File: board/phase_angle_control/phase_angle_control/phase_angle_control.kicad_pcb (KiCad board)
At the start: 4 copper layers, 77.7 x 63.7 mm, 39 parts, among them J1 TB005-762-02BE, J2 TB005-762-02BE, J3 Conn_01x07, J4 Conn_02x04_Odd_Even, J5 Conn_02x04_Odd_Even, J6 Conn_02x04_Odd_Even, J9 Screw_Terminal_01x02, T1 Transformer_1P_1S, U1 STM32G030F6P, U2 PC3H4, U3 MOC3063S-TA1, U4 ACS71240, U7 MAX31855KASA+T

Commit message: Wip3
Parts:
- moved R4 2.66 mm to (114.9, 83.8)
- moved R2 2.48 mm to (118.1, 83.9)
- moved U2 2.33 mm to (116.7, 75.5)
- moved U3 2.22 mm to (124.3, 75.6)
- moved R3 1.95 mm to (125.8, 83.5)
- moved C6 0.60 mm to (132.9, 80.7)
- moved R10 0.41 mm to (135.1, 83.3)
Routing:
- net GND: track 39.1 -> 43.1 mm
- net CURRENT_SENS: track 34.0 -> 30.3 mm
- net zero_crossing: track 49.5 -> 53.1 mm
- net Net-(TRI1-Pad3): track 9.84 -> 12.4 mm
- net AC1: track 26.4 -> 28.3 mm
- net Net-(R3-Pad1): track 3.21 -> 4.81 mm
- net Net-(R1-Pad2): track 3.09 -> 4.37 mm
- net AC2: track 58.9 -> 60.1 mm, vias 26 -> 34
- net Net-(R10-Pad2): track 2.02 -> 2.62 mm
- net AC_LOAD1: vias 16 -> 13
- net AC_LOAD0: vias 14 -> 29
- added copper zone on B.Cu, net +3V3
- added copper zone on F.Cu, net GND

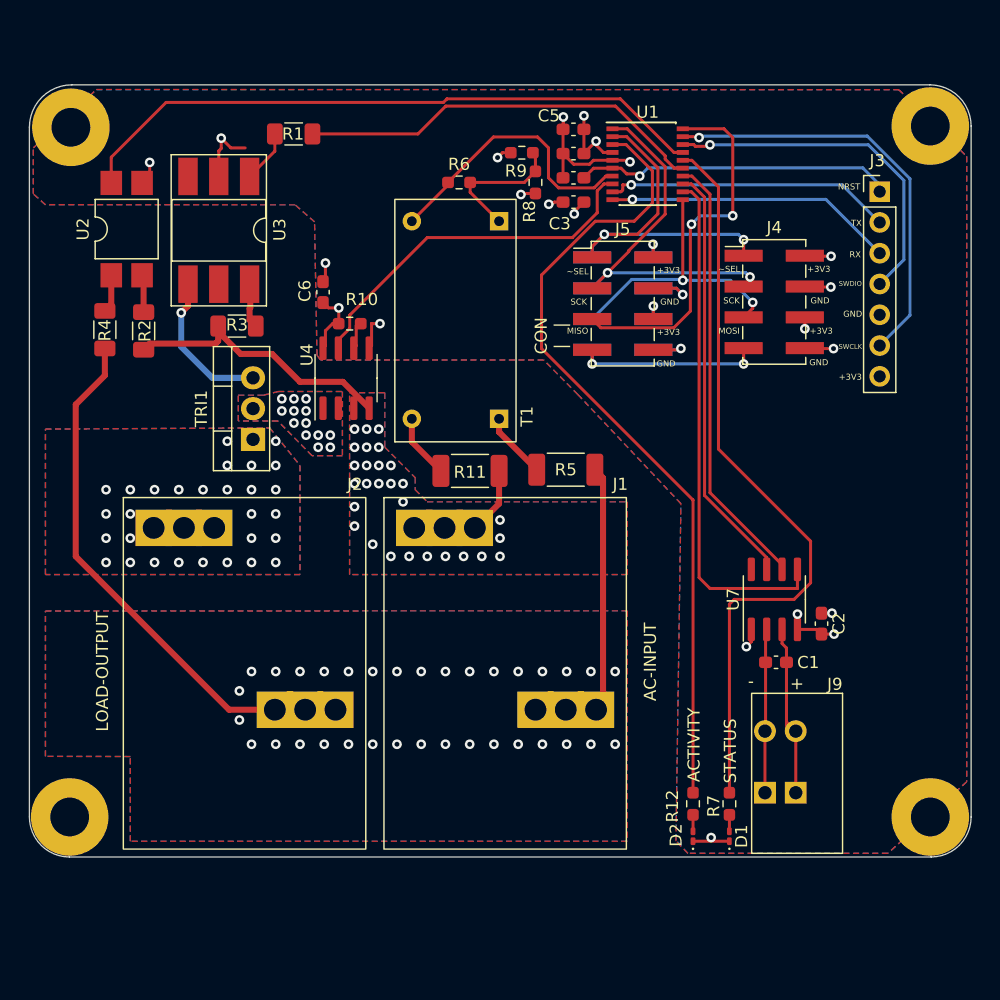
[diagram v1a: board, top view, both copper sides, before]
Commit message: Redesign phase angle contrller board for more current throughput
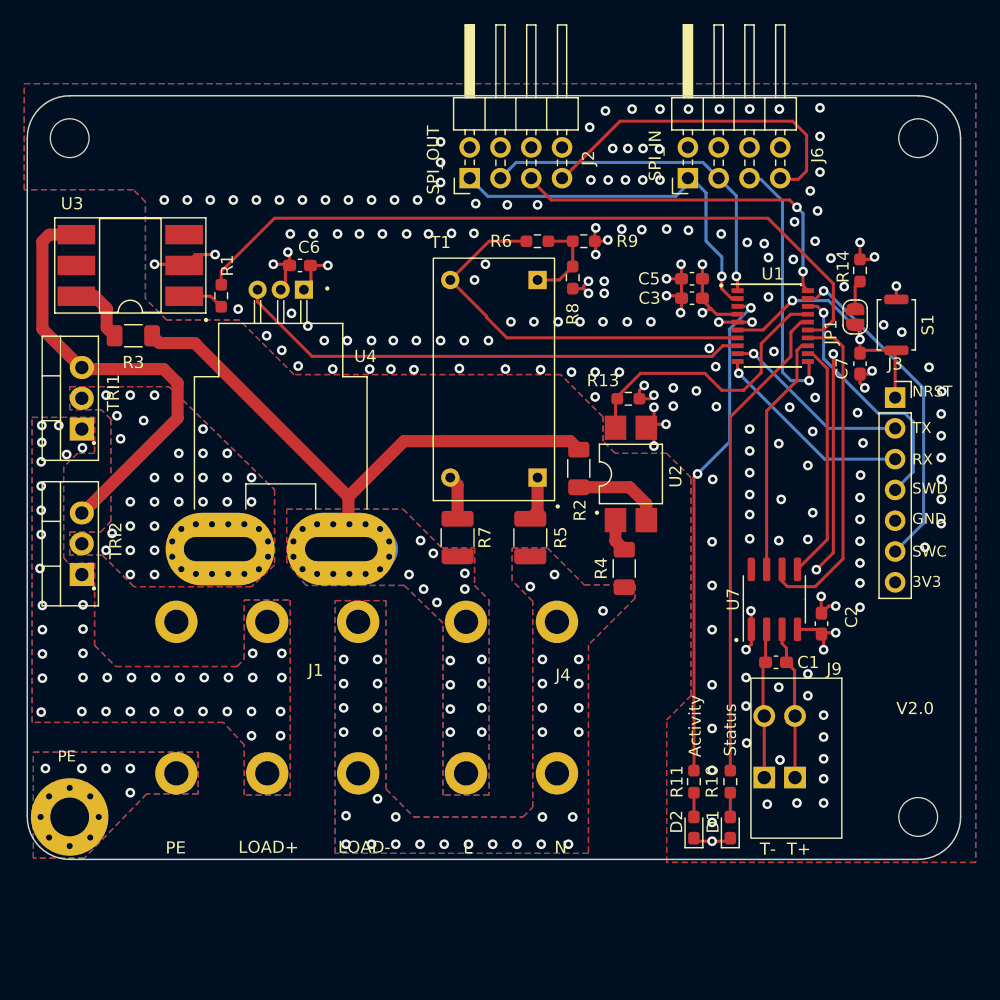
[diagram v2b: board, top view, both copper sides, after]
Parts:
- removed ? (x3): , 
- removed C4: 100nF, Capacitor_SMD:C_0603_1608Metric_Pad1.08x0.95mm_HandSolder
- removed J5: Conn_02x04_Odd_Even, Connector_PinHeader_2.54mm:PinHeader_2x04_P2.54mm_Vertical_SMD
- removed R12: 110, Resistor_SMD:R_0603_1608Metric_Pad0.98x0.95mm_HandSolder
- removed REF**: MountingHole_3.2mm_M3_Pad, MountingHole:MountingHole_3.2mm_M3_Pad
- added JP1: Jumper_2_Open, Jumper:SolderJumper-2_P1.3mm_Open_RoundedPad1.0x1.5mm, F.Cu at (176.8, 82.8)
- added M1: MountingHoles, pac:MountingHolesPE, F.Cu at (112.0, 124.0)
- added R13: 47k, Resistor_SMD:R_0603_1608Metric_Pad0.98x0.95mm_HandSolder, F.Cu at (158.1, 89.5)
- added R14: 330, Resistor_SMD:R_0603_1608Metric_Pad0.98x0.95mm_HandSolder, F.Cu at (177.2, 78.9)
- added S1: B3U-1000P, Button_Switch_SMD:SW_Push_SPST_NO_Alps_SKRK, F.Cu at (180.2, 83.4)
- added TRI2: RS3035H-8A, Package_TO_SOT_THT:TO-220-3_Vertical, F.Cu at (113.0, 104.0)
- D1: value LED_green -> Status; footprint LED_SMD:LED_0201_0603Metric_Pad0.64x0.40mm_HandSolder -> LED_SMD:LED_0603_1608Metric_Pad1.05x0.95mm_HandSolder
- D2: value LED_yellow -> Activity; footprint LED_SMD:LED_0201_0603Metric_Pad0.64x0.40mm_HandSolder -> LED_SMD:LED_0603_1608Metric_Pad1.05x0.95mm_HandSolder
- J1: value TB005-762-02BE -> Screw_Terminal_01x03; footprint pac:con_EB167A-02-H -> pac:KF206B-7.5-3P
- J2: value TB005-762-02BE -> Conn_02x04_Odd_Even; footprint pac:con_EB167A-02-H -> Connector_PinHeader_2.54mm:PinHeader_2x04_P2.54mm_Horizontal
- J3: value Conn_01x07 -> A2541HWV-7P; footprint Connector_PinHeader_2.54mm:PinHeader_1x07_P2.54mm_Vertical -> Connector_PinSocket_2.54mm:PinSocket_1x07_P2.54mm_Vertical
- J4: value Conn_02x04_Odd_Even -> Screw_Terminal_01x02; footprint Connector_PinHeader_2.54mm:PinHeader_2x04_P2.54mm_Vertical_SMD -> pac:KF206B-7.5-2P
- J6: footprint Connector_PinHeader_2.54mm:PinHeader_2x04_P2.54mm_Vertical_SMD -> Connector_PinHeader_2.54mm:PinHeader_2x04_P2.54mm_Horizontal; moved to F.Cu
- J9: value Screw_Terminal_01x02 -> 1-2834016-2
- R1: value 330 -> 110; footprint Resistor_SMD:R_1206_3216Metric_Pad1.30x1.75mm_HandSolder -> Resistor_SMD:R_0603_1608Metric_Pad0.98x0.95mm_HandSolder
- R10: value 10k -> 110
- R11: value 162k -> 110; footprint Resistor_SMD:R_2010_5025Metric_Pad1.40x2.65mm_HandSolder -> Resistor_SMD:R_0603_1608Metric_Pad0.98x0.95mm_HandSolder
- R3: value 330 -> 619
- R5: value 162k -> 280k; footprint Resistor_SMD:R_2010_5025Metric_Pad1.40x2.65mm_HandSolder -> Resistor_SMD:R_1210_3225Metric_Pad1.30x2.65mm_HandSolder
- R6: value 1650 -> 1600
- R7: value 110 -> 280k; footprint Resistor_SMD:R_0603_1608Metric_Pad0.98x0.95mm_HandSolder -> Resistor_SMD:R_1210_3225Metric_Pad1.30x2.65mm_HandSolder
- TRI1: value BTA16-600BWRG -> RS3035H-8A
- U2: value PC3H4 -> EL354N(A)(TA)-VG
- U3: value MOC3063S-TA1 -> MOC3052S-TA1
- U4: value ACS71240 -> ACS758xCB-050B-PFF; footprint Package_SO:SOIC-8_3.9x4.9mm_P1.27mm -> Sensor_Current:Allegro_CB_PFF
- moved R10 49.1 mm to (166.5, 121.1), turned to -90 degrees
- moved R4 47.2 mm to (157.8, 103.5)
- moved U2 46.2 mm to (158.3, 95.7)
- moved J2 44.4 mm to (145.0, 71.3), turned to 90 degrees
- moved J4 39.5 mm to (148.7, 114.7)
- moved R2 37.7 mm to (154.0, 95.2), turned to 90 degrees
- moved R11 31.6 mm to (163.5, 121.1), turned to -90 degrees
- moved R7 31.4 mm to (144.0, 101.0)
- moved C7 28.2 mm to (177.2, 86.6), turned to -90 degrees
- moved J1 19.8 mm to (128.3, 114.3)
- moved J3 17.0 mm to (180.1, 89.4)
- moved U1 16.9 mm to (170.0, 83.5)
- moved C5 15.7 mm to (163.3, 79.6)
- moved R1 14.6 mm to (124.5, 81.0), turned to -90 degrees
- moved TRI1 14.2 mm to (113.0, 92.0)
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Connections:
- J1 pad 1: AC1 -> PE
- J1 pad 2: AC2 -> AC_LOAD0
- J2 pad 1: AC_LOAD0 -> SPI_SEL
- J2 pad 2: AC2 -> +3V3
- J4 pad 1: SPI_SEL -> AC1
- J4 pad 2: +3V3 -> AC2
- J6 pad 1: +3V3 -> SPI_SEL
- J6 pad 2: SPI_SEL -> +3V3
- J6 pad 3: GND -> SPI_SCK
- J6 pad 4: SPI_SCK -> GND
- J6 pad 5: +3V3 -> SPI_MOSI
- J6 pad 6: SPI_MOSI -> +3V3
- J6 pad 7: GND -> RET_MISO
- J6 pad 8: RET_MISO -> GND
- R10 pad 1: +3V3 -> Net-(R10-Pad1)
- R10 pad 2: Net-(R10-Pad2) -> Net-(D1-Pad2)
- R11 pad 1: AC1 -> Net-(R11-Pad1)
- R11 pad 2: Net-(T1-Pad2) -> Net-(D2-Pad2)
- R7 pad 1: Net-(D1-Pad2) -> AC1
- T1 pad 2: Net-(T1-Pad2) -> Net-(R7-Pad2)
- U1 pad 16: Net-(R7-Pad2) -> Net-(R10-Pad1)
- U1 pad 3: Net-(R12-Pad2) -> Net-(R11-Pad1)
- U4 pad 1: AC_LOAD1 -> +3V3
- U4 pad 2: AC_LOAD1 -> GND
- U4 pad 3: AC1 -> CURRENT_SENS
- U4 pad 4: AC1 -> AC_LOAD1
- U4 pad 5: GND -> AC1
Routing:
- net Net-(R12-Pad2): track 66.3 -> 0.00 mm
- net AC2: track 60.1 -> 0.00 mm
- net Net-(R7-Pad2): track 62.6 -> 3.65 mm
- net Net-(R11-Pad1): track 0.00 -> 41.3 mm, vias 0 -> 2
- net Net-(R10-Pad1): track 0.00 -> 40.0 mm
- net zero_crossing: track 53.1 -> 23.4 mm
- net enable_power: track 33.8 -> 61.1 mm
- net Net-(TRI1-Pad3): track 12.4 -> 37.3 mm, vias 1 -> 0
- net AC1: track 28.3 -> 51.8 mm, vias 28 -> 15
- net /Untitled Sheet/CLK: track 42.9 -> 19.3 mm
- net /Untitled Sheet/MISO: track 35.1 -> 20.2 mm
- net CURRENT_SENS: track 30.3 -> 42.8 mm
- net RET_MISO: track 16.1 -> 27.6 mm, vias 2 -> 0
- net VOLTAGE_SENS: track 23.1 -> 33.3 mm
- net GND: track 43.1 -> 52.5 mm, vias 14 -> 189
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- added copper zone on In2.Cu, net +3V3
- added copper zone on B.Cu, net GND
- added copper zone on In1.Cu, net GND
- added copper zone on B.Cu, net PE
- added copper zone on F.Cu, net PE
- added copper zone on In1.Cu, net PE
- added copper zone on In2.Cu, net PE
- removed copper zone on B.Cu, net +3V3
- removed copper zone on In1.Cu, net +3V3
- removed copper zone on In2.Cu, net GND
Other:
- board size 77.7 x 63.7 mm -> 77 x 63 mm
- board text added: "3V3"
- board text added: "CLK"
- board text added: "L"
- board text added: "LOAD+"
- board text added: "LOAD-"
- board text added: "MISO_RET"
- board text added: "N"
- board text added: "PE"
- board text added: "SWC"
- board text added: "SWD"
- board text added: "T+"
- board text added: "T-"
- board text added: "V2.0"
- board text removed: "+"
- board text removed: "+3V3"
- board text removed: "-"
- board text removed: "CON | |"
- board text removed: "SCK"
- board text removed: "SWCLK"
- board text removed: "SWDIO"

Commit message: Update phase-angle-control-board to handle more current
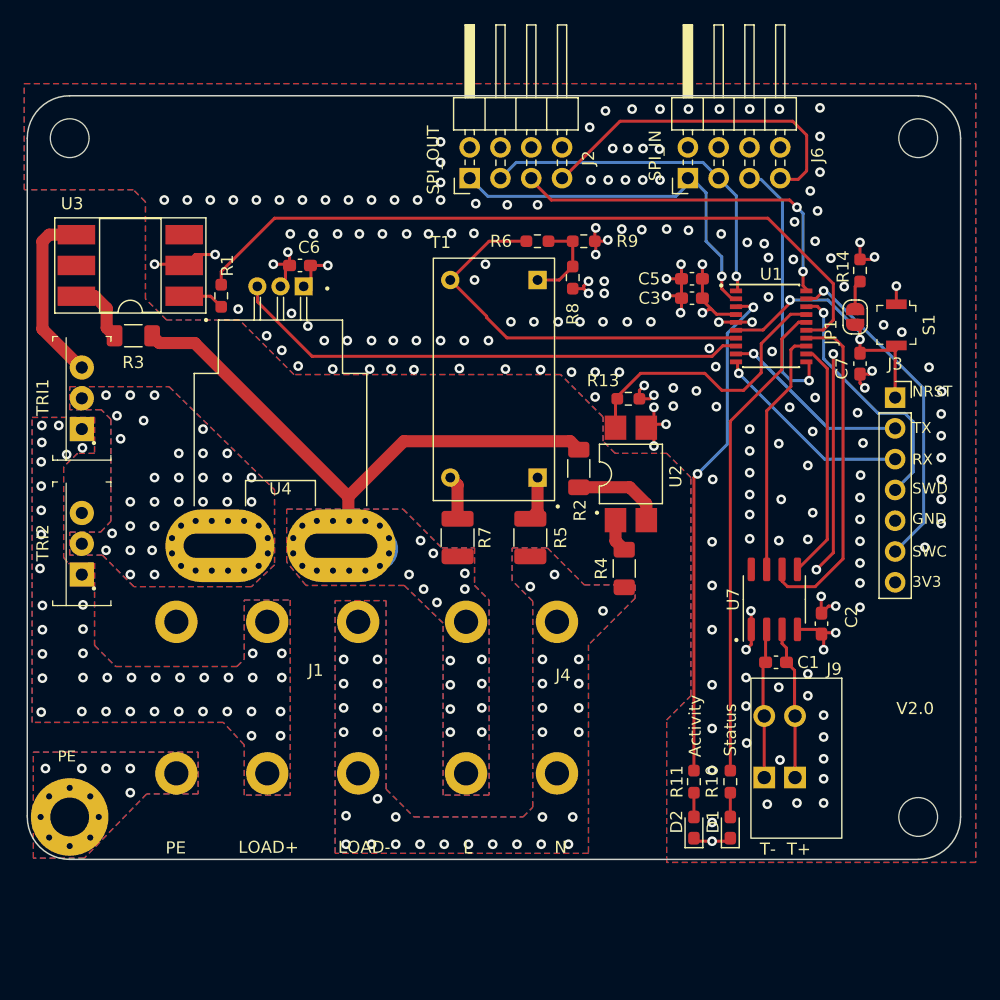
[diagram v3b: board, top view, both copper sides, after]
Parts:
- S1: footprint Button_Switch_SMD:SW_Push_SPST_NO_Alps_SKRK -> digikey-footprints:Switch_Tactile_SMD_B3U-1000P
- TRI1, TRI2: footprint Package_TO_SOT_THT:TO-220-3_Vertical -> digikey-footprints:TO-220-3
- moved U4 0.28 mm to (131.3, 80.2)
- moved U1 0.13 mm to (169.9, 83.5)
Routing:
- net Net-(C1-Pad2): track 13.6 -> 12.7 mm
- net /Untitled Sheet/MISO: track 20.2 -> 20.9 mm

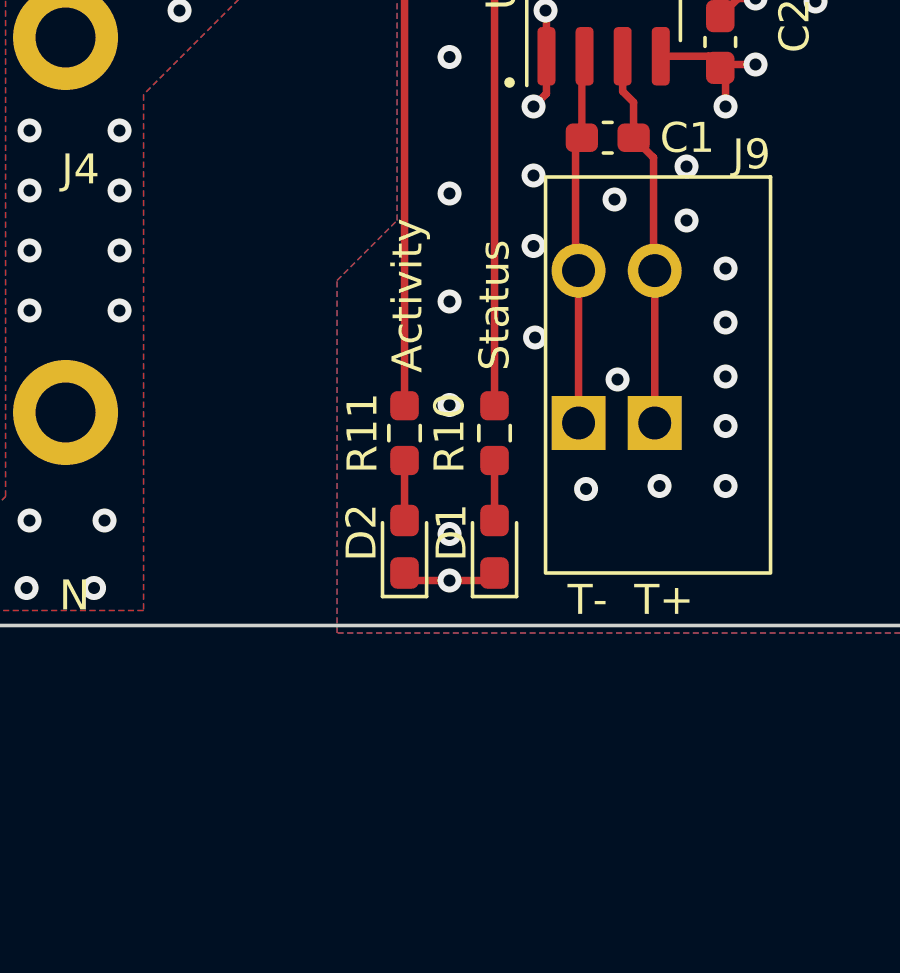
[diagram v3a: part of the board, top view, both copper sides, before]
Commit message: Fix LED rotation
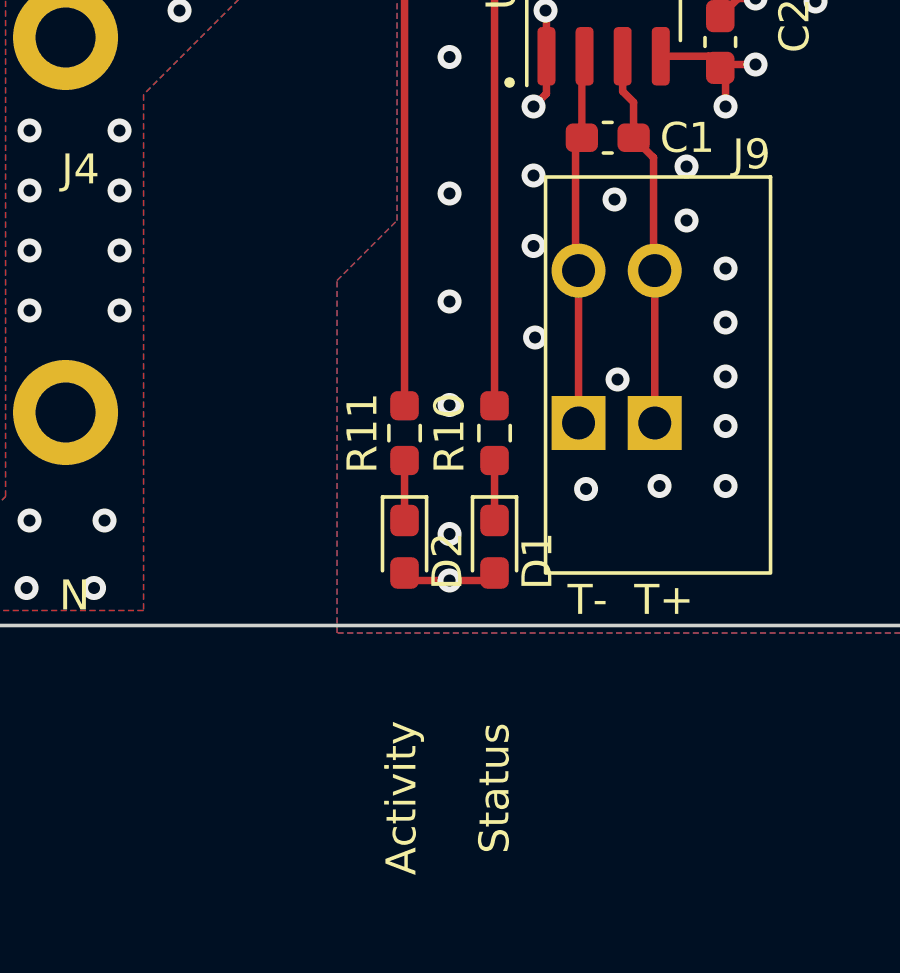
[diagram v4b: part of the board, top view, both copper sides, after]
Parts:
- turned D1 to -90 degrees
- turned D2 to -90 degrees
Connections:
- D1 pad 1: +3V3 -> Net-(D1-Pad1)
- D1 pad 2: Net-(D1-Pad2) -> +3V3
- D2 pad 1: +3V3 -> Net-(R11-Pad2)
- D2 pad 2: Net-(D2-Pad2) -> +3V3
- R10 pad 2: Net-(D1-Pad2) -> Net-(D1-Pad1)
- R11 pad 2: Net-(D2-Pad2) -> Net-(R11-Pad2)
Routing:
- net Net-(R11-Pad2): track 0.00 -> 2.00 mm
- net Net-(D2-Pad2): track 2.00 -> 0.00 mm
- net Net-(D1-Pad2): track 2.00 -> 0.00 mm
- net Net-(D1-Pad1): track 0.00 -> 2.00 mm
